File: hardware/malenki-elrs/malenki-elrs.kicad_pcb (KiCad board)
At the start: 4 copper layers, 19 x 32 mm, 49 parts, among them J1 Conn_01x02_Male-Connector, J2 Conn_01x08_Male, J3 Conn_01x02, J4 Conn_01x02_Male-Connector, J5 Conn_01x02_Male-Connector, J6 Conn_01x02_Male-Connector, U1 A7105, U2 AP2210N-3.3TRG1, U3 ATtiny1616-M, U4 DRV8837DSGR, U5 DRV8837DSGR, U6 DRV8837DSGR, Y1 16mhz Seiko Epson Q24FA20H005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

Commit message: Finalised initial SX1280 schematics, started ESP32 schematic, replace Vreg in schematic
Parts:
- removed AE1: ~, malenki-nano:malenki_antenna
- removed C13, C16, C17, C22, C23, C4: 100nF, Capacitor_SMD:C_0402_1005Metric_Pad0.74x0.62mm_HandSolder
- removed C14, C15: 10pF, Capacitor_SMD:C_0402_1005Metric_Pad0.74x0.62mm_HandSolder
- removed C18: 560pF, Capacitor_SMD:C_0402_1005Metric_Pad0.74x0.62mm_HandSolder
- removed C19: 10nF, Capacitor_SMD:C_0402_1005Metric_Pad0.74x0.62mm_HandSolder
- removed C20, C21: 2.2uF, Capacitor_SMD:C_0603_1608Metric
- removed L1: 2.7nH, Inductor_SMD:L_0402_1005Metric_Pad0.77x0.64mm_HandSolder
- removed L2, L3: 4.7nH, Inductor_SMD:L_0402_1005Metric_Pad0.77x0.64mm_HandSolder
- removed R25: 200R, Resistor_SMD:R_0402_1005Metric
- removed R6: 470R, Resistor_SMD:R_0402_1005Metric
- removed R7, R8: 10k, Resistor_SMD:R_0402_1005Metric
- removed U2: AP2210N-3.3TRG1, Package_TO_SOT_SMD:SOT-23
- removed U3: ATtiny1616-M, Package_DFN_QFN:VQFN-20-1EP_3x3mm_P0.4mm_EP1.7x1.7mm
- removed Y1: 16mhz Seiko Epson Q24FA20H0051200, Crystal:Crystal_SMD_2520-4Pin_2.5x2.0mm
- added ANT1: ANT3216LL00R2400A, malenki-nano:ANT3216LL00R2400A, F.Cu at (115.3, 40.6)
- added C24: 100nF, Capacitor_SMD:C_0402_1005Metric, F.Cu at (120.2, 38.4)
- added C26: 10nF, Capacitor_SMD:C_0402_1005Metric, F.Cu at (120.2, 40.4)
- added C27: 470nF, Capacitor_SMD:C_0402_1005Metric, F.Cu at (120.2, 42.4)
- added C29: 1pF, Capacitor_SMD:C_0402_1005Metric, F.Cu at (120.2, 44.4)
- added C30: 1pF, Capacitor_SMD:C_0402_1005Metric, F.Cu at (116.5, 44.7)
- added C31: 100pF, Capacitor_SMD:C_0402_1005Metric, F.Cu at (120.2, 48.3)
- added C7: 10nF, Capacitor_SMD:C_0402_1005Metric, F.Cu at (120.2, 34.5)
- added C8: 100nF, Capacitor_SMD:C_0402_1005Metric, F.Cu at (120.2, 36.5)
- added L4: 15uH, Inductor_SMD:L_0805_2012Metric, F.Cu at (128.4, 44.5)
- added L5: 3.9nH, Inductor_SMD:L_0402_1005Metric, F.Cu at (127.6, 46.9)
- added R10: 10k, Resistor_SMD:R_0402_1005Metric, F.Cu at (71.0, 67.0)
- added R11: 470R, Resistor_SMD:R_0402_1005Metric, F.Cu at (71.0, 69.0)
- added R12: 470R, Resistor_SMD:R_0402_1005Metric, F.Cu at (71.0, 71.0)
- added R9: 10k, Resistor_SMD:R_0402_1005Metric, F.Cu at (71.0, 65.0)
- added U7: SX1280IMLTRT, malenki-nano:XCVR_SX1280IMLTRT, F.Cu at (101.5, 60.2)
- added U8: ESP32-C3FH4, malenki-nano:QFN50P500X500X90-33N, F.Cu at (79.6, 66.6)
- added Y2: CRYSTAL 52MHz 10pF SMD, Crystal:Crystal_SMD_2520-4Pin_2.5x2.0mm, F.Cu at (123.9, 45.2)
- C10: value 22pF -> 1uF; footprint Capacitor_SMD:C_0402_1005Metric_Pad0.74x0.62mm_HandSolder -> Capacitor_SMD:C_0402_1005Metric
- C11: value 10pF -> 10uF; footprint Capacitor_SMD:C_0402_1005Metric_Pad0.74x0.62mm_HandSolder -> Capacitor_SMD:C_0402_1005Metric
- C12: footprint Capacitor_SMD:C_0402_1005Metric_Pad0.74x0.62mm_HandSolder -> Capacitor_SMD:C_0402_1005Metric
- C9: value 1pF -> 10nF; footprint Capacitor_SMD:C_0402_1005Metric_Pad0.74x0.62mm_HandSolder -> Capacitor_SMD:C_0402_1005Metric
- R5: value 470R -> 499
- U1: value A7105 -> SPX3819M5-L-3-3; footprint malenki-nano:a7105-QFN-20 -> malenki-nano:SOT95P280X145-5N
- moved C10 28.9 mm to (73.8, 65.0), turned to 0 degrees
- moved C11 28.5 mm to (73.8, 66.9), turned to 0 degrees
- moved C9 27.2 mm to (73.8, 63.0), turned to 0 degrees
- moved C12 26.9 mm to (73.8, 68.9), turned to 0 degrees
- moved R5 21.6 mm to (71.0, 63.0), turned to 0 degrees
- moved U1 10.5 mm to (110.0, 68.5), turned to 0 degrees
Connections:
- C10 pad 1: /radio/IMPMATCH -> VLOGIC
- C10 pad 2: /radio/RFI -> GND
- C11 pad 1: /radio/IMPMATCH -> VLOGIC
- C11 pad 2: /radio/RFO -> GND
- C12 pad 1: /radio/REGOA -> VLOGIC
- C9 pad 1: /radio/IMPMATCH -> VLOGIC
- R5 pad 1: WEAPON2 -> Net-(U8-GPIO21/U0TXD)
- R5 pad 2: /W2 -> U0TXD
- U1 pad 1: Net-(U1-RSSI) -> VBAT
- U1 pad 2: Net-(U1-BPBG) -> GND
- U1 pad 3: /radio/RFI -> VBAT
- U1 pad 4: /radio/RFO -> unconnected-(U1-BYP-Pad4)
- U1 pad 5: /radio/VDA2 -> VLOGIC
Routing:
- net (no net): track 0.00 -> 44.7 mm, vias 0 -> 7
- net /radio/REGOA: track 21.6 -> 0.00 mm, vias 3 -> 0
- net SPI_SDIO: track 15.4 -> 0.00 mm, vias 2 -> 0
- net SPI_SCK: track 14.0 -> 0.00 mm, vias 2 -> 0
- net GIO1: track 13.6 -> 0.00 mm, vias 2 -> 0
- net GND: track 53.0 -> 42.1 mm, vias 22 -> 19
- net SPI_SCS: track 8.17 -> 0.00 mm, vias 2 -> 0
- net Net-(U1-XI): track 7.04 -> 0.00 mm
- net Net-(U1-XO): track 5.49 -> 0.00 mm
- net /radio/IMPMATCH: track 4.66 -> 0.00 mm
- net /radio/VDA2: track 3.67 -> 0.00 mm
- net VLOGIC: track 11.8 -> 8.77 mm, vias 7 -> 6
- net /radio/RFO: track 2.56 -> 0.00 mm
- net Net-(U1-VT): track 2.53 -> 0.00 mm
- net Net-(C19-Pad1): track 2.15 -> 0.00 mm
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
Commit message: Completed preliminary schematics
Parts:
- removed C12: 100nF, Capacitor_SMD:C_0402_1005Metric
- added C10: 100nF, Capacitor_SMD:C_0402_1005Metric, F.Cu at (62.4, 67.0)
- added C13: 100nF, Capacitor_SMD:C_0402_1005Metric, F.Cu at (62.4, 69.0)
- added C15: 1uF, Capacitor_SMD:C_0402_1005Metric, F.Cu at (62.4, 76.8)
- added C2: 12pF, Capacitor_SMD:C_0402_1005Metric, F.Cu at (77.9, 66.8)
- added C3: 12pF, Capacitor_SMD:C_0402_1005Metric, F.Cu at (77.9, 64.8)
- added C4: 100nF, Capacitor_SMD:C_0402_1005Metric, F.Cu at (72.9, 54.5)
- added C7: 100nF, Capacitor_SMD:C_0402_1005Metric, F.Cu at (62.4, 74.9)
- added C9: 100nF, Capacitor_SMD:C_0402_1005Metric, F.Cu at (65.9, 67.0)
- added R11: 470, Resistor_SMD:R_0402_1005Metric, F.Cu at (80.0, 56.5)
- added R13: 10k, Resistor_SMD:R_0402_1005Metric, F.Cu at (70.0, 56.5)
- added R14: 470, Resistor_SMD:R_0402_1005Metric, F.Cu at (80.0, 58.0)
- added R15: 10k, Resistor_SMD:R_0402_1005Metric, F.Cu at (117.5, 49.5)
- added R5: 470, Resistor_SMD:R_0402_1005Metric, F.Cu at (77.5, 56.5)
- added R6: 10k, Resistor_SMD:R_0402_1005Metric, F.Cu at (70.0, 54.5)
- added Y1: ECS-400-10-37B2-CKY-TR, malenki-nano:XTAL_ECS-400-10-37B2-CKY-TR, F.Cu at (81.2, 65.5)
- C16: renamed from C7; value 10nF -> 100nF
- C20: renamed from C29; value 1pF -> 10pF
- C23: renamed from C30; value 1pF -> 10pF
- C6: renamed from C9; value 10nF -> 100nF
- J2: value Conn_01x08_Male -> PROG Header; footprint malenki-nano:SOIC_clipProgSmall -> Connector_PinHeader_1.27mm:PinHeader_2x03_P1.27mm_Vertical; moved to F.Cu
- J3: value Conn_01x02 -> Weapons
- R12: renamed from R5; value 499 -> 470
- R9: renamed from R1; value 470R -> 1k
- moved J2 8.76 mm to (83.0, 55.5), turned to 0 degrees
- moved R12 8.23 mm to (77.5, 58.0)
- moved C11 8.17 mm to (65.9, 69.0)
- moved C6 6.69 mm to (72.0, 69.4)
- moved C8 6.69 mm to (72.0, 71.4)
- moved R1 6.69 mm to (69.1, 71.4)
- moved R2 6.69 mm to (69.1, 73.4)
- moved R4 6.69 mm to (69.1, 77.4)
- moved U2 6.69 mm to (77.8, 73.1)
- moved R3 6.69 mm to (69.1, 75.4)
- renumbered C2 to C1, C31 to C17, C26 to C18, C8 to C19, C27 to C21, C24 to C22, C1 to C24, C5 to C25, C6 to C26, C3 to C5, C10 to C8, L4 to L1, L5 to L2, R9 to R1, R2 to R10, R10 to R2, R11 to R3, R12 to R4, R3 to R7, R4 to R8, U8 to U2, U7 to U3
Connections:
- D1 pad 2: BLINKY -> VLOGIC
- D2 pad 2: TXDEBUG -> VLOGIC
- J2 pad 1: VBAT -> ESP_EN
- J2 pad 2: unconnected-(J2-Pin_2-Pad2) -> VLOGIC
- J2 pad 3: GND -> U0TXD
- J2 pad 5: unconnected-(J2-Pin_5-Pad5) -> U0RXD
- J2 pad 6: UPDI -> ESPIO0
- R10 pad 2: GND -> TXDEBUG
- R9 pad 2: GND -> BLINKY
- U2 pad 11: unconnected-(U8-VDD3P3_RTC-Pad11) -> VLOGIC
- U2 pad 15: unconnected-(U8-GPIO9-Pad15) -> Net-(U2-GPIO9)
- U2 pad 17: unconnected-(U8-VDD3P3_CPU-Pad17) -> VLOGIC
- U2 pad 18: unconnected-(U8-VDD_SPI-Pad18) -> VLOGIC
- U2 pad 19: unconnected-(U8-GPIO12/SPIHD-Pad19) -> MOTOR1F
- U2 pad 2: Net-(U8-VDD3P3) -> VLOGIC
- U2 pad 20: unconnected-(U8-GPIO13/SPIWP-Pad20) -> MOTOR1R
- U2 pad 21: unconnected-(U8-GPIO14/SPICS0-Pad21) -> MOTOR2F
- U2 pad 22: unconnected-(U8-GPIO15/SPICLK-Pad22) -> MOTOR2R
- U2 pad 23: unconnected-(U8-GPIO16/SPID-Pad23) -> MOTOR3F
- U2 pad 24: unconnected-(U8-GPIO17/SPIQ-Pad24) -> MOTOR3R
- U2 pad 25: unconnected-(U8-GPIO18/USB_D--Pad25) -> TXDEBUG
- U2 pad 26: unconnected-(U8-GPIO19/USB_D+-Pad26) -> VSENSE
- U2 pad 27: U0RXD -> Net-(U2-GPIO20/U0RXD)
- U2 pad 29: unconnected-(U8-XTAL_N-Pad29) -> Net-(U2-XTAL_N)
- U2 pad 3: Net-(U8-VDD3P3) -> VLOGIC
- U2 pad 30: unconnected-(U8-XTAL_P-Pad30) -> Net-(U2-XTAL_P)
- U2 pad 4: unconnected-(U8-GPIO0/XTAL_32K_P-Pad4) -> /W2
- U2 pad 5: unconnected-(U8-GPIO1/XTAL_32K_N-Pad5) -> /W3
- U2 pad 7: unconnected-(U8-CHIP_EN-Pad7) -> Net-(U2-CHIP_EN)
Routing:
- net VLOGIC: track 8.77 -> 39.8 mm, vias 6 -> 10
- net BLINKY: track 17.6 -> 0.00 mm, vias 4 -> 0
- net TXDEBUG: track 13.4 -> 0.00 mm
- net UPDI: track 8.55 -> 0.00 mm, vias 2 -> 0
- net VBAT: track 34.2 -> 32.7 mm

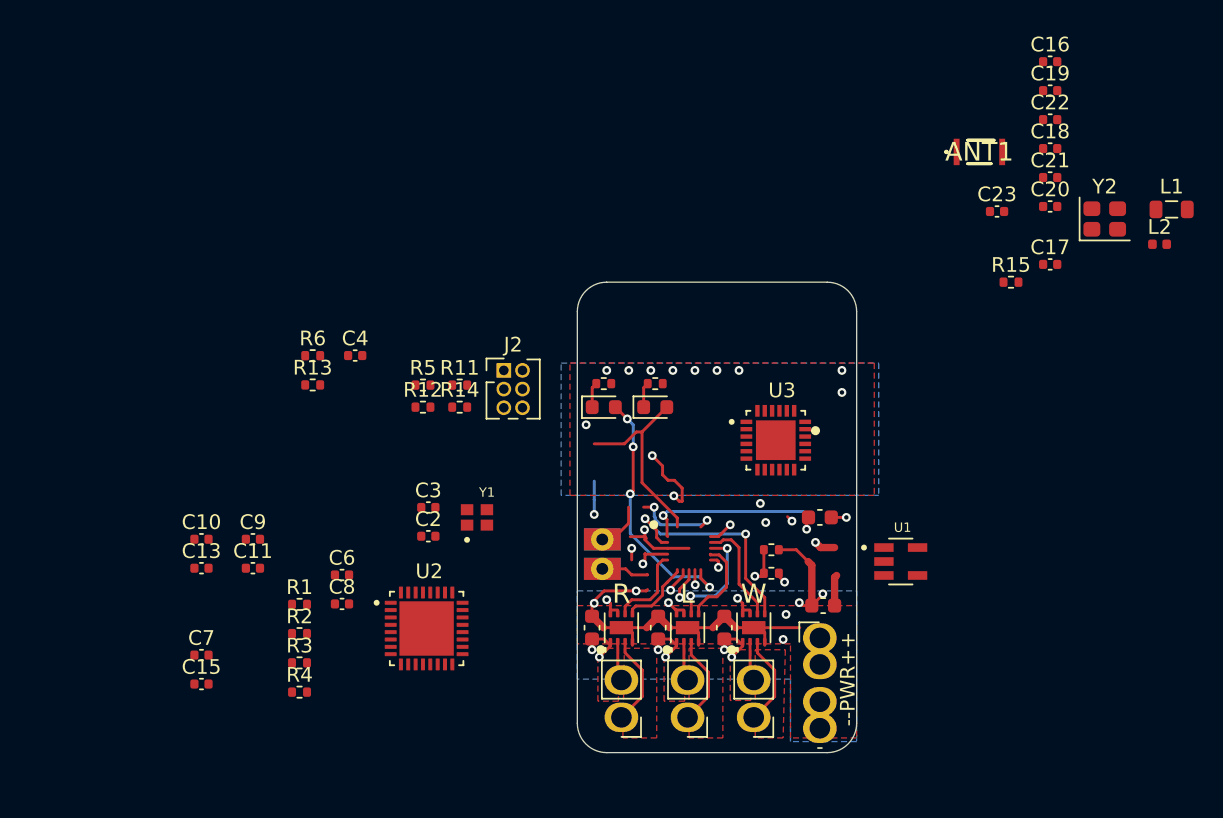
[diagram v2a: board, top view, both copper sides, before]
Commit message: Placing components for ESP and SX1280
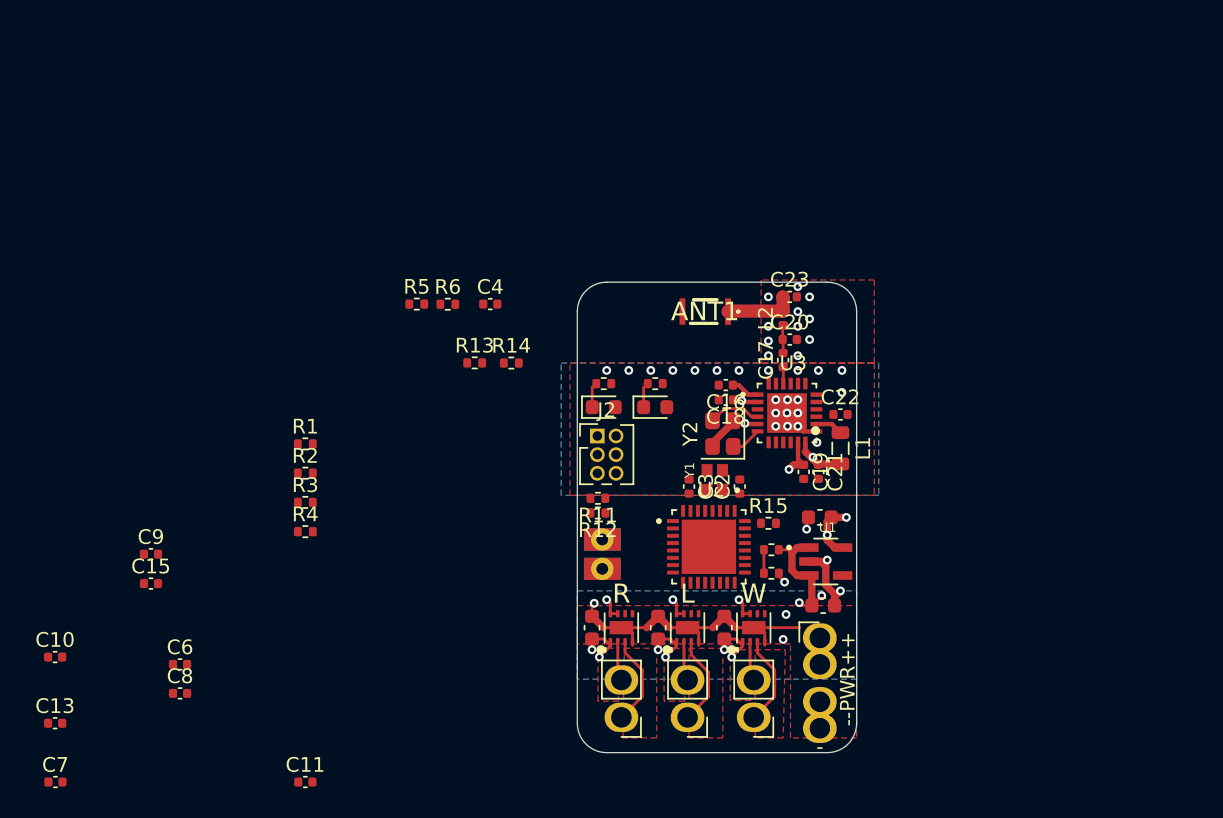
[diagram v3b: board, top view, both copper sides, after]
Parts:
- moved C16 31.2 mm to (98.1, 56.5), turned to 180 degrees
- moved C19 30.9 mm to (103.4, 62.4), turned to -90 degrees
- moved Y2 29.8 mm to (97.9, 59.8), turned to 90 degrees
- moved C18 27.9 mm to (98.1, 57.5), turned to 180 degrees
- moved L1 27.8 mm to (105.9, 60.8), turned to -90 degrees
- moved L2 26.1 mm to (102.0, 52.0), turned to 90 degrees
- moved C21 25.5 mm to (104.4, 62.4), turned to -90 degrees
- moved C22 24.6 mm to (105.9, 58.5)
- moved R15 23.3 mm to (101.0, 65.9)
- moved ANT1 21.6 mm to (96.7, 51.5), turned to 180 degrees
- moved C2 21.5 mm to (99.0, 63.4), turned to 90 degrees
- moved U2 20.0 mm to (97.0, 67.5)
- moved C20 19.9 mm to (102.5, 53.4)
- moved C17 19.3 mm to (102.0, 54.8), turned to 90 degrees
- moved C3 17.8 mm to (95.6, 63.4), turned to -90 degrees
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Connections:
- net DIO2 renamed /radio/DIO2
- net DIO3 renamed /radio/DIO3
- net Net-(ANT1-Pad1) renamed /radio/RF
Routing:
- net (no net): track 44.7 -> 0.00 mm, vias 7 -> 0
- net VLOGIC: track 39.8 -> 11.4 mm, vias 10 -> 6
- net MOTOR1F: track 15.5 -> 0.00 mm, vias 2 -> 0
- net VBAT: track 32.7 -> 20.4 mm, vias 9 -> 8
- net Net-(U3-DCC_FB): track 0.00 -> 11.9 mm, vias 0 -> 2
- net /W2: track 9.83 -> 0.00 mm, vias 2 -> 0
- net MOTOR2R: track 7.39 -> 0.00 mm, vias 2 -> 0
- net MOTOR1R: track 7.01 -> 0.00 mm
- net GND: track 42.1 -> 35.3 mm, vias 19 -> 41
- net VSENSE: track 7.64 -> 1.60 mm, vias 2 -> 0
- net /W3: track 6.01 -> 0.00 mm, vias 2 -> 0
- net MOTOR2F: track 5.74 -> 0.00 mm
- net MOTOR3R: track 5.54 -> 0.00 mm
- net MOTOR3F: track 4.90 -> 0.00 mm
- net /radio/RF: track 0.00 -> 4.74 mm
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
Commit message: Preliminary board layout complete
Awaiting reviewers and preparations for PCBA
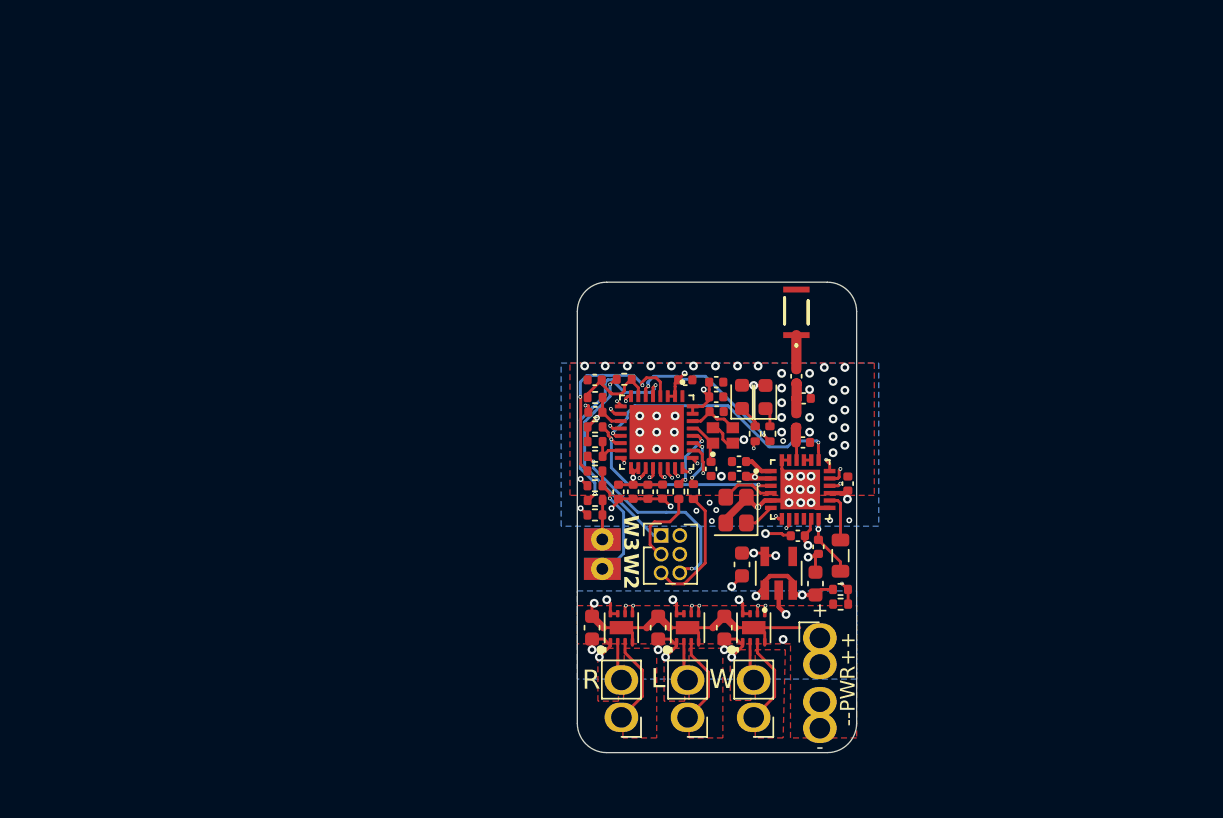
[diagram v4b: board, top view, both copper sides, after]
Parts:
- moved C7 50.8 mm to (95.3, 56.1)
- moved C13 42.4 mm to (89.2, 58.3), turned to 180 degrees
- moved C8 42.2 mm to (97.5, 56.3)
- moved C10 40.9 mm to (91.8, 63.8), turned to -90 degrees
- moved C6 40.8 mm to (97.5, 57.3)
- moved C9 34.1 mm to (92.8, 63.8), turned to -90 degrees
- moved C15 32.4 mm to (90.8, 63.8), turned to -90 degrees
- moved C11 31.3 mm to (93.8, 63.7), turned to -90 degrees
- moved R1 19.9 mm to (89.2, 63.3), turned to 180 degrees
- moved R2 19.9 mm to (89.2, 65.3), turned to 180 degrees
- moved R4 19.8 mm to (89.2, 64.3), turned to 180 degrees
- moved R3 19.8 mm to (89.2, 62.3), turned to 180 degrees
- moved R5 15.0 mm to (91.2, 56.1)
- moved R15 13.5 mm to (89.2, 59.3)
- moved R6 11.9 mm to (89.2, 57.3)
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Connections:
- ANT1 pad 1: /radio/RF -> Net-(ANT1-Pad1)
- C17 pad 1: Net-(U3-RFIO) -> Net-(C17-Pad1)
- C17 pad 2: Net-(C17-Pad2) -> Net-(ANT1-Pad1)
- C20 pad 1: Net-(C17-Pad2) -> Net-(U3-RFIO)
- C23 pad 1: /radio/RF -> Net-(C17-Pad1)
- L2 pad 1: Net-(C17-Pad2) -> Net-(U3-RFIO)
- L2 pad 2: /radio/RF -> Net-(C17-Pad1)
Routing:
- net MOTOR1F: track 0.00 -> 22.4 mm, vias 0 -> 2
- net MOTOR1R: track 0.00 -> 21.7 mm, vias 0 -> 2
- net ESP_SCK: track 0.00 -> 21.0 mm, vias 0 -> 2
- net ESP_MOSI: track 0.00 -> 20.8 mm, vias 0 -> 2
- net ESP_MISO: track 0.00 -> 19.1 mm, vias 0 -> 2
- net VLOGIC: track 11.4 -> 29.9 mm, vias 6 -> 12
- net ESP_NSS: track 0.00 -> 18.2 mm, vias 0 -> 2
- net VSENSE: track 1.60 -> 17.9 mm, vias 0 -> 2
- net BUSY: track 0.00 -> 16.0 mm, vias 0 -> 2
- net ESP_NRESET: track 0.00 -> 15.1 mm, vias 0 -> 2
- net DIO1: track 0.00 -> 14.9 mm, vias 0 -> 2
- net MOTOR2F: track 0.00 -> 14.5 mm, vias 0 -> 2
- net /W3: track 0.00 -> 14.4 mm, vias 0 -> 2
- net MOTOR3R: track 0.00 -> 14.2 mm, vias 0 -> 2
- net ESPIO0: track 0.00 -> 14.1 mm, vias 0 -> 2
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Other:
- board text added: "W2"
- board text added: "W3"
- board text removed: "W2-"
- board text removed: "W3-"

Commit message: minor changes ready for final checks
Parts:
- removed C11: 10uF, Capacitor_SMD:C_0402_1005Metric
- removed C17: 100pF, Capacitor_SMD:C_0402_1005Metric
- R3, R4: value 470R -> 470
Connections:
- C23 pad 1: Net-(C17-Pad1) -> Net-(ANT1-Pad1)
- L2 pad 2: Net-(C17-Pad1) -> Net-(ANT1-Pad1)
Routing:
- net VBAT: track 17.0 -> 20.5 mm
- net GND: track 47.0 -> 49.1 mm, vias 69 -> 70
- net Net-(C17-Pad1): track 2.05 -> 0.00 mm
- net Net-(ANT1-Pad1): track 2.32 -> 4.37 mm
- net VSENSE: track 17.9 -> 16.9 mm, vias 2 -> 3
- net BLINKY: track 11.5 -> 12.2 mm
- net VLOGIC: track 29.9 -> 30.4 mm, vias 12 -> 14
- added copper zone on F.Cu, net unconnected-(ANT1-Pad2)
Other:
- board text added: "Malenki-Nano Integrated ExpressLRS Receiver"
- board text removed: "Malenki-Nano Integrated R"
